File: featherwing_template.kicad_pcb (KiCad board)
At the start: 2 copper layers, 50.8 x 22.9 mm, 6 parts, among them J1 Conn_01x16_Socket, J2 Conn_01x12_Socket

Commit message: Add known nets to the sockets
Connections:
- J1 pad 1: unconnected-(J1-Pin_1-Pad1) -> /RST
- J1 pad 11: unconnected-(J1-Pin_11-Pad11) -> /SCK
- J1 pad 12: unconnected-(J1-Pin_12-Pad12) -> /MO
- J1 pad 13: unconnected-(J1-Pin_13-Pad13) -> /MI
- J1 pad 14: unconnected-(J1-Pin_14-Pad14) -> /RX
- J1 pad 15: unconnected-(J1-Pin_15-Pad15) -> /TX
- J1 pad 2: unconnected-(J1-Pin_2-Pad2) -> +3.3V
- J1 pad 4: unconnected-(J1-Pin_4-Pad4) -> GND
- J2 pad 1: unconnected-(J2-Pin_1-Pad1) -> +BATT
- J2 pad 11: unconnected-(J2-Pin_11-Pad11) -> /SCL
- J2 pad 12: unconnected-(J2-Pin_12-Pad12) -> /SDA
- J2 pad 2: unconnected-(J2-Pin_2-Pad2) -> /EN
- J2 pad 3: unconnected-(J2-Pin_3-Pad3) -> /USB
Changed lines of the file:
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@@
 	(net 2 "unconnected-(J1-Pin_9-Pad9)")
 	(net 3 "unconnected-(J1-Pin_10-Pad10)")
-	(net 4 "unconnected-(J1-Pin_4-Pad4)")
+	(net 4 "/SCK")
 	(net 5 "unconnected-(J1-Pin_6-Pad6)")
 	(net 6 "unconnected-(J1-Pin_7-Pad7)")
-	(net 7 "unconnected-(J1-Pin_11-Pad11)")
-	(net 8 "unconnected-(J1-Pin_15-Pad15)")
-	(net 9 "unconnected-(J1-Pin_14-Pad14)")
+	(net 7 "/TX")
+	(net 8 "/RX")
+	(net 9 "/MO")
 	(net 10 "unconnected-(J1-Pin_8-Pad8)")
 	(net 11 "unconnected-(J1-Pin_5-Pad5)")
-	(net 12 "unconnected-(J1-Pin_12-Pad12)")
+	(net 12 "/RST")
 	(net 13 "unconnected-(J1-Pin_3-Pad3)")
-	(net 14 "unconnected-(J1-Pin_1-Pad1)")
+	(net 14 "+3.3V")
 	(net 15 "unconnected-(J1-Pin_16-Pad16)")
-	(net 16 "unconnected-(J1-Pin_2-Pad2)")
-	(net 17 "unconnected-(J1-Pin_13-Pad13)")
+	(net 16 "/MI")
+	(net 17 "/SDA")
 	(net 18 "unconnected-(J2-Pin_5-Pad5)")
 	(net 19 "unconnected-(J2-Pin_6-Pad6)")
-	(net 20 "unconnected-(J2-Pin_12-Pad12)")
-	(net 21 "unconnected-(J2-Pin_1-Pad1)")
+	(net 20 "+BATT")
+	(net 21 "/EN")
 	(net 22 "unconnected-(J2-Pin_7-Pad7)")
-	(net 23 "unconnected-(J2-Pin_2-Pad2)")
+	(net 23 "/SCL")
 	(net 24 "unconnected-(J2-Pin_8-Pad8)")
-	(net 25 "unconnected-(J2-Pin_11-Pad11)")
-	(net 26 "unconnected-(J2-Pin_3-Pad3)")
-	(net 27 "unconnected-(J2-Pin_10-Pad10)")
-	(net 28 "unconnected-(J2-Pin_4-Pad4)")
-	(net 29 "unconnected-(J2-Pin_9-Pad9)")
+	(net 25 "/USB")
+	(net 26 "unconnected-(J2-Pin_10-Pad10)")
+	(net 27 "unconnected-(J2-Pin_4-Pad4)")
+	(net 28 "unconnected-(J2-Pin_9-Pad9)")
 	(footprint "Connector_PinSocket_2.54mm:PinSocket_1x16_P2.54mm_Vertical"
 		(layer "F.Cu")
@@
 			(layers "*.Cu" "*.Mask")
 			(remove_unused_layers no)
-			(net 14 "unconnected-(J1-Pin_1-Pad1)")
+			(net 12 "/RST")
 			(pinfunction "Pin_1")
 			(pintype "passive")
@@
 			(layers "*.Cu" "*.Mask")
 			(remove_unused_layers no)
-			(net 16 "unconnected-(J1-Pin_2-Pad2)")
+			(net 14 "+3.3V")
 			(pinfunction "Pin_2")
 			(pintype "passive")
@@
 			(layers "*.Cu" "*.Mask")
 			(remove_unused_layers no)
-			(net 4 "unconnected-(J1-Pin_4-Pad4)")
+			(net 1 "GND")
 			(pinfunction "Pin_4")
 			(pintype "passive")
@@
 			(layers "*.Cu" "*.Mask")
 			(remove_unused_layers no)
-			(net 7 "unconnected-(J1-Pin_11-Pad11)")
+			(net 4 "/SCK")
 			(pinfunction "Pin_11")
 			(pintype "passive")
@@
 			(layers "*.Cu" "*.Mask")
 			(remove_unused_layers no)
-			(net 12 "unconnected-(J1-Pin_12-Pad12)")
+			(net 9 "/MO")
 			(pinfunction "Pin_12")
 			(pintype "passive")
@@
 			(layers "*.Cu" "*.Mask")
 			(remove_unused_layers no)
-			(net 17 "unconnected-(J1-Pin_13-Pad13)")
+			(net 16 "/MI")
 			(pinfunction "Pin_13")
 			(pintype "passive")
@@
 			(layers "*.Cu" "*.Mask")
 			(remove_unused_layers no)
-			(net 9 "unconnected-(J1-Pin_14-Pad14)")
+			(net 8 "/RX")
 			(pinfunction "Pin_14")
 			(pintype "passive")
@@
 			(layers "*.Cu" "*.Mask")
 			(remove_unused_layers no)
-			(net 8 "unconnected-(J1-Pin_15-Pad15)")
+			(net 7 "/TX")
 			(pinfunction "Pin_15")
 			(pintype "passive")
@@
 			(layers "*.Cu" "*.Mask")
 			(remove_unused_layers no)
-			(net 21 "unconnected-(J2-Pin_1-Pad1)")
+			(net 20 "+BATT")
 			(pinfunction "Pin_1")
 			(pintype "passive")
@@
 			(layers "*.Cu" "*.Mask")
 			(remove_unused_layers no)
-			(net 23 "unconnected-(J2-Pin_2-Pad2)")
+			(net 21 "/EN")
 			(pinfunction "Pin_2")
 			(pintype "passive")
@@
 			(layers "*.Cu" "*.Mask")
 			(remove_unused_layers no)
-			(net 26 "unconnected-(J2-Pin_3-Pad3)")
+			(net 25 "/USB")
 			(pinfunction "Pin_3")
 			(pintype "passive")
@@
 			(layers "*.Cu" "*.Mask")
 			(remove_unused_layers no)
-			(net 28 "unconnected-(J2-Pin_4-Pad4)")
+			(net 27 "unconnected-(J2-Pin_4-Pad4)")
 			(pinfunction "Pin_4")
 			(pintype "passive")
@@
 			(layers "*.Cu" "*.Mask")
 			(remove_unused_layers no)
-			(net 29 "unconnected-(J2-Pin_9-Pad9)")
+			(net 28 "unconnected-(J2-Pin_9-Pad9)")
 			(pinfunction "Pin_9")
 			(pintype "passive")
@@
 			(layers "*.Cu" "*.Mask")
 			(remove_unused_layers no)
-			(net 27 "unconnected-(J2-Pin_10-Pad10)")
+			(net 26 "unconnected-(J2-Pin_10-Pad10)")
 			(pinfunction "Pin_10")
 			(pintype "passive")
@@
 			(layers "*.Cu" "*.Mask")
 			(remove_unused_layers no)
-			(net 25 "unconnected-(J2-Pin_11-Pad11)")
+			(net 23 "/SCL")
 			(pinfunction "Pin_11")
 			(pintype "passive")
@@
 			(layers "*.Cu" "*.Mask")
 			(remove_unused_layers no)
-			(net 20 "unconnected-(J2-Pin_12-Pad12)")
+			(net 17 "/SDA")
 			(pinfunction "Pin_12")
 			(pintype "passive")

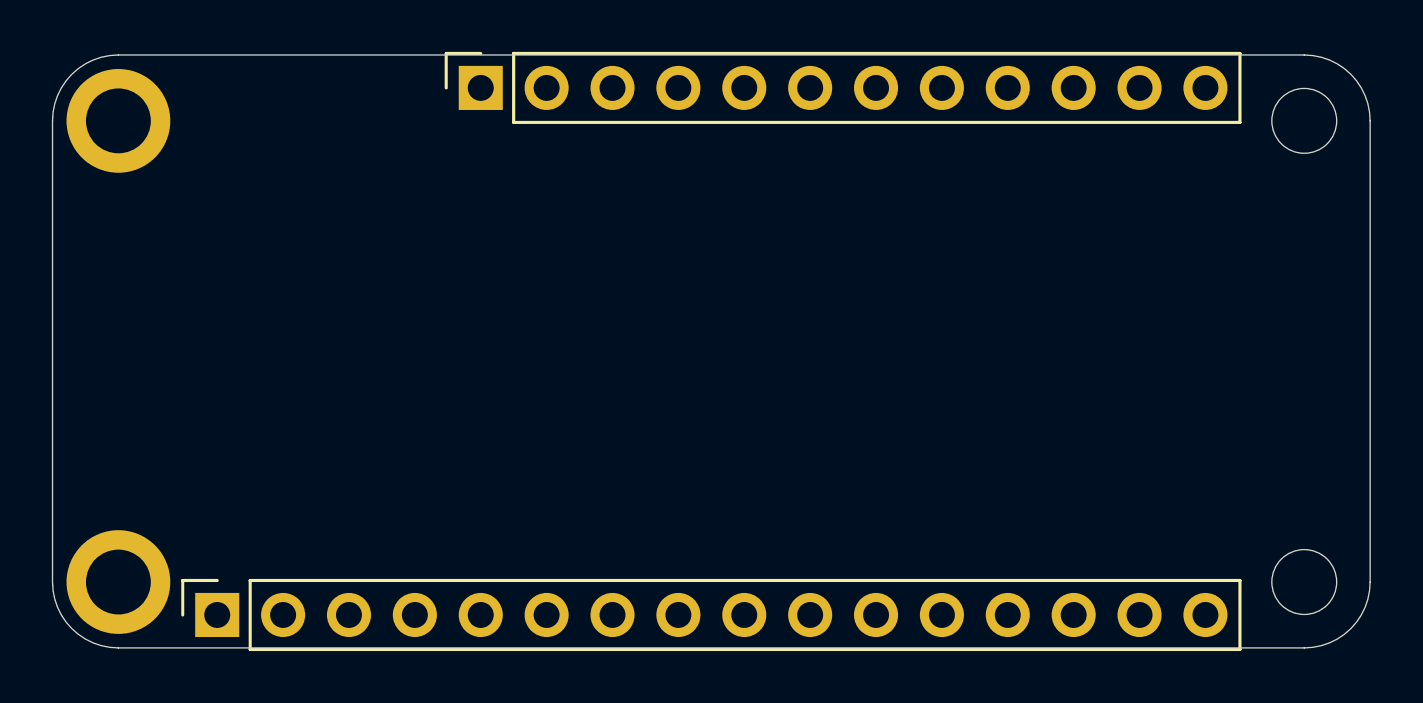
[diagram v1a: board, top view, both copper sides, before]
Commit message: Add copper pours that match the board size
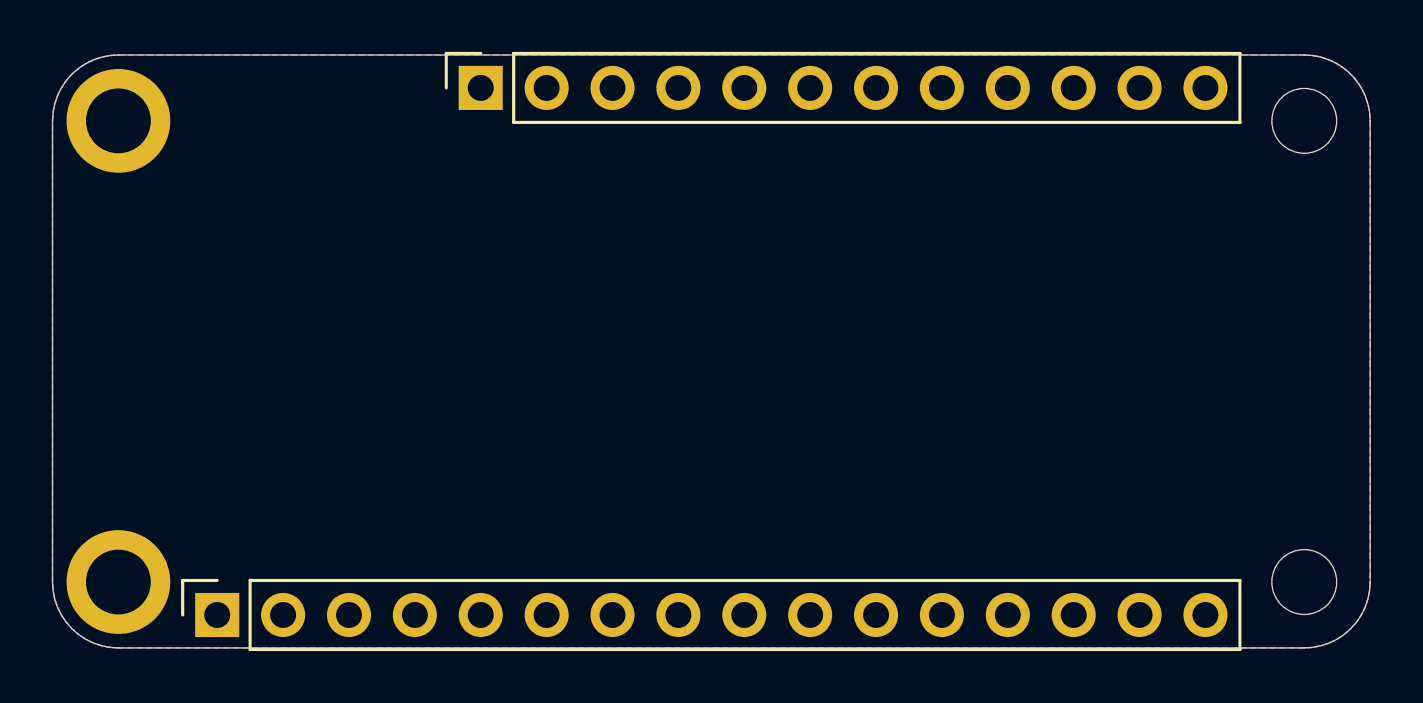
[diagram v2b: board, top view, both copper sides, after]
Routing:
- added copper zone on B.Cu, net GND
- added copper zone on F.Cu, net GND
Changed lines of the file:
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@@
 		(allow_soldermask_bridges_in_footprints no)
 		(tenting front back)
+		(grid_origin 125.65 96.13)
 		(pcbplotparams
 			(layerselection 0x00000000_00000000_55555555_5755f5ff)
@@
 		(layer "Edge.Cuts")
 	)
+	(zone
+		(net 1)
+		(net_name "GND")
+		(layer "F.Cu")
+		(hatch edge 0.508)
+		(connect_pads
+			(clearance 0.508)
+		)
+		(min_thickness 0.254)
+		(filled_areas_thickness no)
+		(fill yes
+			(thermal_gap 0.508)
+			(thermal_bridge_width 0.508)
+		)
+		(polygon
+			(pts
+				(xy 173.901 113.894) (xy 173.883 114.2) (xy 173.827 114.501) (xy 173.736 114.794) (xy 173.61 115.074)
+				(xy 173.451 115.336) (xy 173.262 115.578) (xy 173.045 115.795) (xy 172.804 115.984) (xy 172.541 116.143)
+				(xy 172.262 116.269) (xy 171.969 116.36) (xy 171.667 116.415) (xy 171.361 116.434) (xy 125.641 116.434)
+				(xy 125.335 116.415) (xy 125.033 116.36) (xy 124.74 116.269) (xy 124.461 116.143) (xy 124.198 115.984)
+				(xy 123.957 115.795) (xy 123.74 115.578) (xy 123.551 115.336) (xy 123.392 115.074) (xy 123.266 114.794)
+				(xy 123.175 114.501) (xy 123.12 114.2) (xy 123.101 113.894) (xy 123.101 96.114) (xy 123.12 95.807)
+				(xy 123.175 95.506) (xy 123.266 95.213) (xy 123.392 94.933) (xy 123.551 94.671) (xy 123.74 94.429)
+				(xy 123.957 94.212) (xy 124.198 94.023) (xy 124.461 93.865) (xy 124.74 93.739) (xy 125.033 93.647)
+				(xy 125.335 93.592) (xy 125.641 93.574) (xy 171.361 93.574) (xy 171.667 93.592) (xy 171.969 93.647)
+				(xy 172.262 93.739) (xy 172.541 93.865) (xy 172.804 94.023) (xy 173.045 94.212) (xy 173.262 94.429)
+				(xy 173.451 94.671) (xy 173.61 94.933) (xy 173.736 95.213) (xy 173.827 95.506) (xy 173.883 95.807)
+				(xy 173.901 96.114)
+			)
+		)
+	)
+	(zone
+		(net 1)
+		(net_name "GND")
+		(layer "B.Cu")
+		(hatch edge 0.508)
+		(connect_pads
+			(clearance 0.508)
+		)
+		(min_thickness 0.254)
+		(filled_areas_thickness no)
+		(fill yes
+			(thermal_gap 0.508)
+			(thermal_bridge_width 0.508)
+		)
+		(polygon
+			(pts
+				(xy 173.901 113.894) (xy 173.883 114.2) (xy 173.827 114.501) (xy 173.736 114.794) (xy 173.61 115.074)
+				(xy 173.451 115.336) (xy 173.262 115.578) (xy 173.045 115.795) (xy 172.804 115.984) (xy 172.541 116.143)
+				(xy 172.262 116.269) (xy 171.969 116.36) (xy 171.667 116.415) (xy 171.361 116.434) (xy 125.641 116.434)
+				(xy 125.335 116.415) (xy 125.033 116.36) (xy 124.74 116.269) (xy 124.461 116.143) (xy 124.198 115.984)
+				(xy 123.957 115.795) (xy 123.74 115.578) (xy 123.551 115.336) (xy 123.392 115.074) (xy 123.266 114.794)
+				(xy 123.175 114.501) (xy 123.12 114.2) (xy 123.101 113.894) (xy 123.101 96.114) (xy 123.12 95.807)
+				(xy 123.175 95.506) (xy 123.266 95.213) (xy 123.392 94.933) (xy 123.551 94.671) (xy 123.74 94.429)
+				(xy 123.957 94.212) (xy 124.198 94.023) (xy 124.461 93.865) (xy 124.74 93.739) (xy 125.033 93.647)
+				(xy 125.335 93.592) (xy 125.641 93.574) (xy 171.361 93.574) (xy 171.667 93.592) (xy 171.969 93.647)
+				(xy 172.262 93.739) (xy 172.541 93.865) (xy 172.804 94.023) (xy 173.045 94.212) (xy 173.262 94.429)
+				(xy 173.451 94.671) (xy 173.61 94.933) (xy 173.736 95.213) (xy 173.827 95.506) (xy 173.883 95.807)
+				(xy 173.901 96.114)
+			)
+		)
+	)
 	(embedded_fonts no)
